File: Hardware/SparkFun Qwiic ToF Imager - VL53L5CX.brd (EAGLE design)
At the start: 25.4 x 25.4 mm, 63 parts, among them J3 PTH, U1 VL53L5CX

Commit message: Add production files post design review
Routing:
- net N$4: track 12.0 -> 9.91 mm
- net GND: track 0.00 -> 1.25 mm, vias 12 -> 16
- net VDDA: track 42.7 -> 43.8 mm
- net VDDIO: track 51.3 -> 51.5 mm, vias 5 -> 4

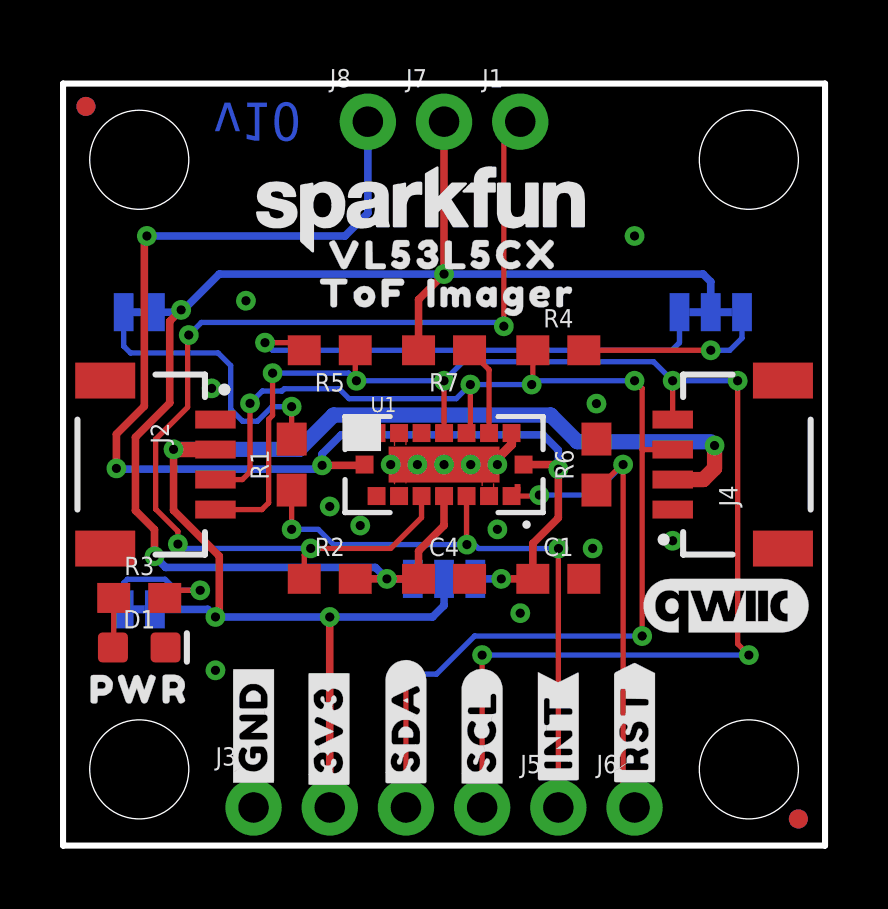
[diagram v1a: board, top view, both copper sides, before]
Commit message: Reduce copper and paste aperatures on VL53L5CX FP.
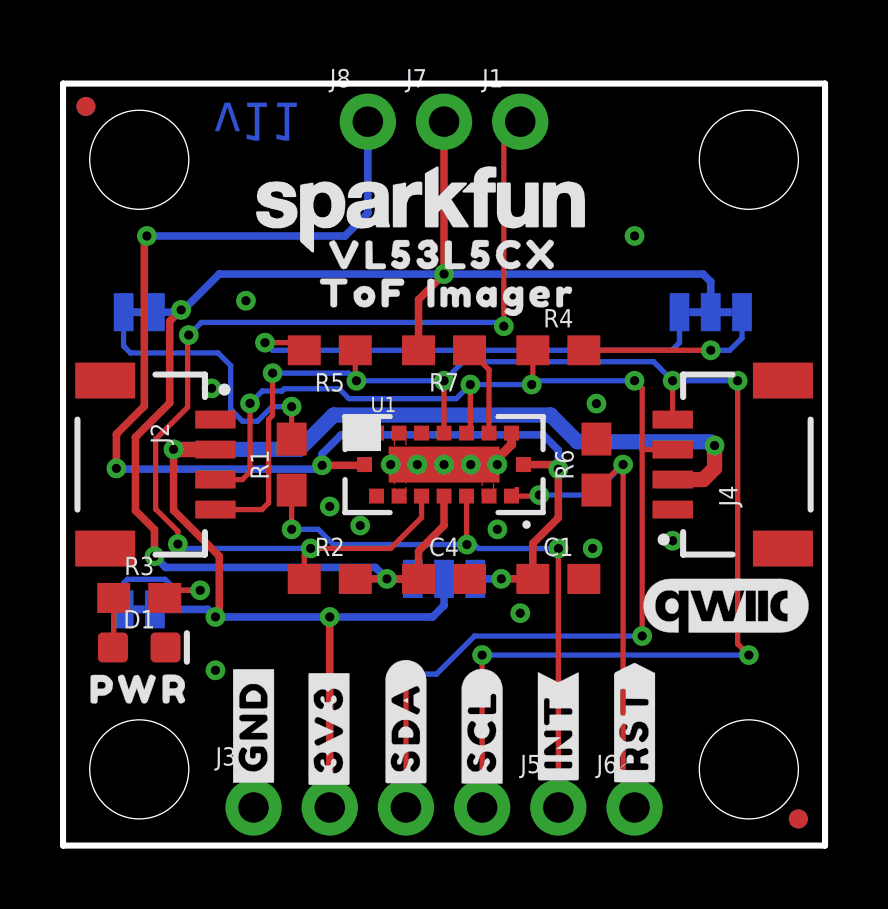
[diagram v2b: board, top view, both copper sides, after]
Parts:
- I2C: value (none) -> JUMPER-SMT_3_2-NC_TRACE_SILK
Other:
- board text added: "v11"
- board text removed: "v10"
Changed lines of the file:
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@@
 <layer number="29" name="tStop" color="7" fill="3" visible="no" active="yes"/>
 <layer number="30" name="bStop" color="7" fill="6" visible="no" active="yes"/>
-<layer number="31" name="tCream" color="7" fill="4" visible="no" active="yes"/>
+<layer number="31" name="tCream" color="7" fill="4" visible="yes" active="yes"/>
 <layer number="32" name="bCream" color="7" fill="5" visible="no" active="yes"/>
 <layer number="33" name="tFinish" color="6" fill="3" visible="no" active="yes"/>
@@
 <wire x1="25.4" y1="25.4" x2="25.4" y2="0" width="0.2032" layer="20"/>
 <wire x1="25.4" y1="0" x2="0" y2="0" width="0.2032" layer="20"/>
-<text x="6.477" y="24.13" size="1.27" layer="16" font="vector" ratio="15" rot="SMR180" align="center">v10</text>
+<text x="6.477" y="24.13" size="1.27" layer="16" font="vector" ratio="15" rot="SMR180" align="center">v11</text>
 <text x="15.24" y="-8.89" size="1.778" layer="51">N. Seidle</text>
 <dimension x1="2.54" y1="22.86" x2="22.86" y2="22.86" x3="12.7" y3="27.94" textsize="1.778" layer="47" unit="inch"/>
@@
 <attribute name="VALUE" x="8.89" y="17.272" size="0.6096" layer="27" font="vector" ratio="20" rot="R180" align="top-center"/>
 </element>
-<element name="I2C" library="SparkFun-Jumpers" package="SMT-JUMPER_3_2-NC_TRACE_SILK" package3d_urn="urn:adsk.eagle:package:39289/1" value="" x="21.59" y="17.78" smashed="yes" rot="MR180">
+<element name="I2C" library="SparkFun-Jumpers" package="SMT-JUMPER_3_2-NC_TRACE_SILK" package3d_urn="urn:adsk.eagle:package:39289/1" value="JUMPER-SMT_3_2-NC_TRACE_SILK" x="21.59" y="17.78" smashed="yes" rot="MR180">
 <attribute name="NAME" x="21.59" y="16.637" size="0.6096" layer="26" font="vector" ratio="20" rot="MR180" align="bottom-center"/>
 <attribute name="VALUE" x="21.59" y="18.923" size="0.6096" layer="28" font="vector" ratio="20" rot="MR180" align="top-center"/>

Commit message: Add panel files for v1.1
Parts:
- removed U$13: (no value), output:ADR#0X520
- added U$27: (no value), output:ARD#0X290
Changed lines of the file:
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@@
 <layer number="29" name="tStop" color="7" fill="3" visible="no" active="yes"/>
 <layer number="30" name="bStop" color="7" fill="6" visible="no" active="yes"/>
-<layer number="31" name="tCream" color="7" fill="4" visible="yes" active="yes"/>
+<layer number="31" name="tCream" color="7" fill="4" visible="no" active="yes"/>
 <layer number="32" name="bCream" color="7" fill="5" visible="no" active="yes"/>
 <layer number="33" name="tFinish" color="6" fill="3" visible="no" active="yes"/>
@@
 <attribute name="VALUE" x="2.54" y="9.017" size="0.6096" layer="28" font="vector" ratio="20" rot="MR180" align="top-center"/>
 </element>
-<element name="U$13" library="output" package="ADR#0X520" value="" x="20.32" y="8.89" smashed="yes" rot="MR0"/>
 <element name="R6" library="SparkFun-Resistors" package="0603" value="47k" x="17.78" y="12.7" smashed="yes" rot="R90">
 <attribute name="NAME" x="17.018" y="12.7" size="0.6096" layer="25" font="vector" ratio="20" rot="R90" align="bottom-center"/>
@@
 <element name="U$24" library="output" package="#SCL#1" value="" x="13.97" y="3.81" smashed="yes" rot="MR270"/>
 <element name="U$25" library="output" package="#SDA#0" value="" x="11.43" y="3.937" smashed="yes" rot="MR270"/>
+<element name="U$27" library="output" package="ARD#0X290" value="" x="20.32" y="8.89" smashed="yes" rot="MR0"/>
 </elements>
 <signals>
